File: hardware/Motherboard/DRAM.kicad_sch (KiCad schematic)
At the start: 42 parts, among them U11 74LS245, U12 74LS541, U13 74LS541, U14 74LS541, U15 74LS393, U16 MK4164N, U17 MK4164N, U18 MK4164N, U19 MK4164N, U20 MK4164N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

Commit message: Footprints.
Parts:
- C17, C18, C19, C20, C21, C22, C23, C24, C25, C26, C27, C28, C29, C30, C31, C36, C72: footprint (none) -> Capacitor_THT:C_Disc_D9.0mm_W2.5mm_P5.00mm
- C3, C4: footprint (none) -> Capacitor_THT:C_Disc_D3.0mm_W1.6mm_P2.50mm
- R22, R48: footprint (none) -> Resistor_THT:R_Axial_DIN0309_L9.0mm_D3.2mm_P12.70mm_Horizontal
- U11, U12, U13, U14: footprint (none) -> Package_DIP:DIP-20_W7.62mm_Socket
- U15, U24, U25, U26, U28, U29, U7, U71, U8: footprint (none) -> Package_DIP:DIP-14_W7.62mm_Socket
- U16, U17, U18, U19, U20, U21, U22, U23: footprint Package_DIP:DIP-16_W7.62mm -> Package_DIP:DIP-16_W7.62mm_Socket
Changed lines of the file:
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@@
 			)
 		)
-		(property "Footprint" ""
+		(property "Footprint" "Package_DIP:DIP-14_W7.62mm_Socket"
 			(at 241.3 172.72 0)
 			(effects
@@
 			)
 		)
-		(property "Footprint" "Package_DIP:DIP-16_W7.62mm"
+		(property "Footprint" "Package_DIP:DIP-16_W7.62mm_Socket"
 			(at 363.22 123.698 0)
 			(effects
@@
 			)
 		)
-		(property "Footprint" ""
+		(property "Footprint" "Capacitor_THT:C_Disc_D9.0mm_W2.5mm_P5.00mm"
 			(at 398.4752 49.53 0)
 			(effects
@@
 			)
 		)
-		(property "Footprint" "Package_DIP:DIP-16_W7.62mm"
+		(property "Footprint" "Package_DIP:DIP-16_W7.62mm_Socket"
 			(at 363.22 71.628 0)
 			(effects
@@
 			)
 		)
-		(property "Footprint" "Package_DIP:DIP-16_W7.62mm"
+		(property "Footprint" "Package_DIP:DIP-16_W7.62mm_Socket"
 			(at 294.64 71.628 0)
 			(effects
@@
 			)
 		)
-		(property "Footprint" ""
+		(property "Footprint" "Resistor_THT:R_Axial_DIN0309_L9.0mm_D3.2mm_P12.70mm_Horizontal"
 			(at 90.932 184.15 90)
 			(effects
@@
 			)
 		)
-		(property "Footprint" "Package_DIP:DIP-16_W7.62mm"
+		(property "Footprint" "Package_DIP:DIP-16_W7.62mm_Socket"
 			(at 363.22 175.768 0)
 			(effects
@@
 			)
 		)
-		(property "Footprint" ""
+		(property "Footprint" "Resistor_THT:R_Axial_DIN0309_L9.0mm_D3.2mm_P12.70mm_Horizontal"
 			(at 90.932 224.79 90)
 			(effects
@@
 			)
 		)
-		(property "Footprint" ""
+		(property "Footprint" "Package_DIP:DIP-14_W7.62mm_Socket"
 			(at 266.7 229.87 0)
 			(effects
@@
 			)
 		)
-		(property "Footprint" ""
+		(property "Footprint" "Capacitor_THT:C_Disc_D9.0mm_W2.5mm_P5.00mm"
 			(at 93.6752 102.87 0)
 			(effects
@@
 			)
 		)
-		(property "Footprint" ""
+		(property "Footprint" "Package_DIP:DIP-14_W7.62mm_Socket"
 			(at 266.7 245.11 0)
 			(effects
@@
 			)
 		)
-		(property "Footprint" ""
+		(property "Footprint" "Capacitor_THT:C_Disc_D9.0mm_W2.5mm_P5.00mm"
 			(at 74.6252 102.87 0)
 			(effects
@@
 			)
 		)
-		(property "Footprint" ""
+		(property "Footprint" "Capacitor_THT:C_Disc_D9.0mm_W2.5mm_P5.00mm"
 			(at 176.2252 132.08 0)
 			(effects
@@
 			)
 		)
-		(property "Footprint" ""
+		(property "Footprint" "Package_DIP:DIP-14_W7.62mm_Socket"
 			(at 27.94 158.75 0)
 			(effects
@@
 			)
 		)
-		(property "Footprint" ""
+		(property "Footprint" "Package_DIP:DIP-14_W7.62mm_Socket"
 			(at 241.3 147.32 0)
 			(effects
@@
 			)
 		)
-		(property "Footprint" ""
+		(property "Footprint" "Package_DIP:DIP-20_W7.62mm_Socket"
 			(at 142.24 102.87 0)
 			(effects
@@
 			)
 		)
-		(property "Footprint" ""
+		(property "Footprint" "Package_DIP:DIP-14_W7.62mm_Socket"
 			(at 30.48 241.3 0)
 			(effects
@@
 			)
 		)
-		(property "Footprint" ""
+		(property "Footprint" "Capacitor_THT:C_Disc_D9.0mm_W2.5mm_P5.00mm"
 			(at 78.4352 250.19 0)
 			(effects
@@
 			)
 		)
-		(property "Footprint" ""
+		(property "Footprint" "Package_DIP:DIP-14_W7.62mm_Socket"
 			(at 49.53 241.3 0)
 			(effects
@@
 			)
 		)
-		(property "Footprint" ""
+		(property "Footprint" "Capacitor_THT:C_Disc_D9.0mm_W2.5mm_P5.00mm"
 			(at 266.3952 104.14 0)
 			(effects
@@
 			)
 		)
-		(property "Footprint" ""
+		(property "Footprint" "Package_DIP:DIP-14_W7.62mm_Socket"
 			(at 45.72 190.5 0)
 			(effects
@@
 			)
 		)
-		(property "Footprint" ""
+		(property "Footprint" "Capacitor_THT:C_Disc_D9.0mm_W2.5mm_P5.00mm"
 			(at 266.3952 205.74 0)
 			(effects
@@
 			)
 		)
-		(property "Footprint" ""
+		(property "Footprint" "Package_DIP:DIP-14_W7.62mm_Socket"
 			(at 222.25 271.78 0)
 			(effects
@@
 			)
 		)
-		(property "Footprint" ""
+		(property "Footprint" "Package_DIP:DIP-14_W7.62mm_Socket"
 			(at 76.2 158.75 0)
 			(effects
@@
 			)
 		)
-		(property "Footprint" "Package_DIP:DIP-16_W7.62mm"
+		(property "Footprint" "Package_DIP:DIP-16_W7.62mm_Socket"
 			(at 294.64 175.768 0)
 			(effects
@@
 			)
 		)
-		(property "Footprint" ""
+		(property "Footprint" "Package_DIP:DIP-14_W7.62mm_Socket"
 			(at 114.3 198.12 0)
 			(effects
@@
 			)
 		)
-		(property "Footprint" ""
+		(property "Footprint" "Capacitor_THT:C_Disc_D9.0mm_W2.5mm_P5.00mm"
 			(at 33.9852 102.87 0)
 			(effects
@@
 			)
 		)
-		(property "Footprint" ""
+		(property "Footprint" "Package_DIP:DIP-14_W7.62mm_Socket"
 			(at 114.3 238.76 0)
 			(effects
@@
 			)
 		)
-		(property "Footprint" ""
+		(property "Footprint" "Package_DIP:DIP-14_W7.62mm_Socket"
 			(at 175.26 227.33 0)
 			(effects
@@
 			)
 		)
-		(property "Footprint" ""
+		(property "Footprint" "Capacitor_THT:C_Disc_D9.0mm_W2.5mm_P5.00mm"
 			(at 398.4752 205.74 0)
 			(effects
@@
 			)
 		)
-		(property "Footprint" ""
+		(property "Footprint" "Package_DIP:DIP-14_W7.62mm_Socket"
 			(at 52.07 158.75 0)
 			(effects
@@
 			)
 		)
-		(property "Footprint" ""
+		(property "Footprint" "Package_DIP:DIP-14_W7.62mm_Socket"
 			(at 199.39 227.33 0)
 			(effects
@@
 			)
 		)
-		(property "Footprint" ""
+		(property "Footprint" "Capacitor_THT:C_Disc_D9.0mm_W2.5mm_P5.00mm"
 			(at 398.4752 153.67 0)
 			(effects
@@
 			)
 		)
-		(property "Footprint" ""
+		(property "Footprint" "Package_DIP:DIP-14_W7.62mm_Socket"
 			(at 219.71 227.33 0)
 			(effects
@@
 			)
 		)
-		(property "Footprint" ""
+		(property "Footprint" "Capacitor_THT:C_Disc_D9.0mm_W2.5mm_P5.00mm"
 			(at 266.3952 151.13 0)
 			(effects
@@
 			)
 		)
-		(property "Footprint" ""
+		(property "Footprint" "Capacitor_THT:C_Disc_D9.0mm_W2.5mm_P5.00mm"
 			(at 60.6552 149.86 0)
 			(effects
@@
 			)
 		)
-		(property "Footprint" ""
+		(property "Footprint" "Package_DIP:DIP-14_W7.62mm_Socket"
 			(at 142.24 209.55 0)
 			(effects
@@
 			)
 		)
-		(property "Footprint" ""
+		(property "Footprint" "Package_DIP:DIP-14_W7.62mm_Socket"
 			(at 26.67 118.11 0)
 			(effects
@@
 			)
 		)
-		(property "Footprint" ""
+		(property "Footprint" "Package_DIP:DIP-14_W7.62mm_Socket"
 			(at 46.99 118.11 0)
 			(effects
@@
 			)
 		)
-		(property "Footprint" ""
+		(property "Footprint" "Package_DIP:DIP-14_W7.62mm_Socket"
 			(at 86.36 118.11 0)
 			(effects
@@
 			)
 		)
-		(property "Footprint" ""
+		(property "Footprint" "Capacitor_THT:C_Disc_D9.0mm_W2.5mm_P5.00mm"
 			(at 36.5252 149.86 0)
 			(effects
@@
 			)
 		)
-		(property "Footprint" ""
+		(property "Footprint" "Capacitor_THT:C_Disc_D3.0mm_W1.6mm_P2.50mm"
 			(at 93.6752 195.58 0)
 			(effects
@@
 			)
 		)
-		(property "Footprint" ""
+		(property "Footprint" "Package_DIP:DIP-14_W7.62mm_Socket"
 			(at 246.38 271.78 0)
 			(effects
@@
 			)
 		)
-		(property "Footprint" ""
+		(property "Footprint" "Capacitor_THT:C_Disc_D9.0mm_W2.5mm_P5.00mm"
 			(at 266.3952 53.34 0)
 			(effects
@@
 			)
 		)
-		(property "Footprint" ""
+		(property "Footprint" "Package_DIP:DIP-20_W7.62mm_Socket"
 			(at 190.5 157.48 0)
 			(effects
@@
 			)
 		)
-		(property "Footprint" ""
+		(property "Footprint" "Capacitor_THT:C_Disc_D3.0mm_W1.6mm_P2.50mm"
 			(at 93.6752 236.22 0)
 			(effects
@@
 			)
 		)
-		(property "Footprint" "Package_DIP:DIP-16_W7.62mm"
+		(property "Footprint" "Package_DIP:DIP-16_W7.62mm_Socket"
 			(at 294.64 123.698 0)
 			(effects
@@
 			)
 		)
-		(property "Footprint" ""
+		(property "Footprint" "Package_DIP:DIP-14_W7.62mm_Socket"
 			(at 66.04 241.3 0)
 			(effects
@@
 			)
 		)
-		(property "Footprint" ""
+		(property "Footprint" "Capacitor_THT:C_Disc_D9.0mm_W2.5mm_P5.00mm"
 			(at 54.3052 102.87 0)
 			(effects
@@
 			)
 		)
-		(property "Footprint" ""
+		(property "Footprint" "Package_DIP:DIP-14_W7.62mm_Socket"
 			(at 161.29 266.7 0)
 			(effects
@@
 			)
 		)
-		(property "Footprint" ""
+		(property "Footprint" "Capacitor_THT:C_Disc_D9.0mm_W2.5mm_P5.00mm"
 			(at 398.4752 101.6 0)
 			(effects
@@
 			)
 		)
-		(property "Footprint" ""
+		(property "Footprint" "Package_DIP:DIP-14_W7.62mm_Socket"
 			(at 64.77 209.55 0)
 			(effects
@@
 			)
 		)
-		(property "Footprint" "Package_DIP:DIP-16_W7.62mm"
+		(property "Footprint" "Package_DIP:DIP-16_W7.62mm_Socket"
 			(at 294.64 227.838 0)
 			(effects
@@
 			)
 		)
-		(property "Footprint" ""
+		(property "Footprint" "Capacitor_THT:C_Disc_D9.0mm_W2.5mm_P5.00mm"
 			(at 127.9652 81.28 0)
 			(effects
@@
 			)
 		)
-		(property "Footprint" ""
+		(property "Footprint" "Package_DIP:DIP-20_W7.62mm_Socket"
 			(at 142.24 46.99 0)
 			(effects
@@
 			)
 		)
-		(property "Footprint" ""
+		(property "Footprint" "Package_DIP:DIP-14_W7.62mm_Socket"
 			(at 67.31 118.11 0)
 			(effects
@@
 			)
 		)
-		(property "Footprint" ""
+		(property "Footprint" "Package_DIP:DIP-14_W7.62mm_Socket"
 			(at 204.47 257.81 0)
 			(effects
@@
 			)
 		)
-		(property "Footprint" ""
+		(property "Footprint" "Package_DIP:DIP-20_W7.62mm_Socket"
 			(at 142.24 157.48 0)
 			(effects
@@
 			)
 		)
-		(property "Footprint" "Package_DIP:DIP-16_W7.62mm"
+		(property "Footprint" "Package_DIP:DIP-16_W7.62mm_Socket"
 			(at 363.22 227.838 0)
 			(effects

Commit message: Fix DRAM address bus connection.
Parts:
- U24: footprint Package_DIP:DIP-14_W7.62mm_Socket -> Package_DIP:DIP-16_W7.62mm_Socket
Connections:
- net RA0: now also U16.5 (A0), U17.5 (A0), U18.5 (A0), U19.5 (A0), U20.5 (A0), U21.5 (A0), U22.5 (A0), U23.5 (A0)
- net RA1: now also U16.7 (A1), U17.7 (A1), U18.7 (A1), U19.7 (A1), U20.7 (A1), U21.7 (A1), U22.7 (A1), U23.7 (A1)
- net RA2: now also U16.6 (A2), U17.6 (A2), U18.6 (A2), U19.6 (A2), U20.6 (A2), U21.6 (A2), U22.6 (A2), U23.6 (A2)
- net RA3: now also U16.12 (A3), U17.12 (A3), U18.12 (A3), U19.12 (A3), U20.12 (A3), U21.12 (A3), U22.12 (A3), U23.12 (A3)
- net RA4: now also U16.11 (A4), U17.11 (A4), U18.11 (A4), U19.11 (A4), U20.11 (A4), U21.11 (A4), U22.11 (A4), U23.11 (A4)
- net RA5: now also U16.10 (A5), U17.10 (A5), U18.10 (A5), U19.10 (A5), U20.10 (A5), U21.10 (A5), U22.10 (A5), U23.10 (A5)
- net RA6: now also U16.13 (A6), U17.13 (A6), U18.13 (A6), U19.13 (A6), U20.13 (A6), U21.13 (A6), U22.13 (A6), U23.13 (A6)
- net RA7: now also U16.9 (A7), U17.9 (A7), U18.9 (A7), U19.9 (A7), U20.9 (A7), U21.9 (A7), U22.9 (A7), U23.9 (A7)

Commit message: Fix DRAM address bits ordering.
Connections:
- net RA0: now also U16.13 (A6), U17.13 (A6), U19.13 (A6), U20.13 (A6), U21.13 (A6), U22.13 (A6), U23.13 (A6); no longer U16.5 (A0), U17.5 (A0), U18.5 (A0), U19.5 (A0), U20.5 (A0), U21.5 (A0), U22.5 (A0), U23.5 (A0)
- net RA1: now also U16.12 (A3), U17.12 (A3), U19.12 (A3), U20.12 (A3), U21.12 (A3), U22.12 (A3), U23.12 (A3); no longer U16.7 (A1), U17.7 (A1), U18.7 (A1), U19.7 (A1), U20.7 (A1), U21.7 (A1), U22.7 (A1), U23.7 (A1)
- net RA2: now also U16.5 (A0), U17.5 (A0), U19.5 (A0), U20.5 (A0), U21.5 (A0), U22.5 (A0), U23.5 (A0); no longer U16.6 (A2), U17.6 (A2), U18.6 (A2), U19.6 (A2), U20.6 (A2), U21.6 (A2), U22.6 (A2), U23.6 (A2)
- net RA3: now also U16.11 (A4), U17.11 (A4), U19.11 (A4), U20.11 (A4), U21.11 (A4), U22.11 (A4), U23.11 (A4); no longer U16.12 (A3), U17.12 (A3), U18.12 (A3), U19.12 (A3), U20.12 (A3), U21.12 (A3), U22.12 (A3), U23.12 (A3)
- net RA4: now also U16.6 (A2), U17.6 (A2), U19.6 (A2), U20.6 (A2), U21.6 (A2), U22.6 (A2), U23.6 (A2); no longer U16.11 (A4), U17.11 (A4), U18.11 (A4), U19.11 (A4), U20.11 (A4), U21.11 (A4), U22.11 (A4), U23.11 (A4)
- net RA5: no longer U18.10 (A5)
- net RA6: now also U16.7 (A1), U17.7 (A1), U19.7 (A1), U20.7 (A1), U21.7 (A1), U22.7 (A1), U23.7 (A1); no longer U16.13 (A6), U17.13 (A6), U18.13 (A6), U19.13 (A6), U20.13 (A6), U21.13 (A6), U22.13 (A6), U23.13 (A6)
- net RA7: no longer U18.9 (A7)

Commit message: missing addresses?
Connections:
- net RA0: now also U18.13 (A6)
- net RA1: now also U18.12 (A3)
- net RA2: now also U18.5 (A0)
- net RA3: now also U18.11 (A4)
- net RA4: now also U18.6 (A2)
- net RA5: now also U18.10 (A5)
- net RA6: now also U18.7 (A1)
- net RA7: now also U18.9 (A7)

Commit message: more fixes !
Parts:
- C28: now not fitted
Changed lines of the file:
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@@
 		(in_bom yes)
 		(on_board yes)
-		(dnp no)
+		(dnp yes)
 		(fields_autoplaced yes)
 		(property "Reference" "C28"

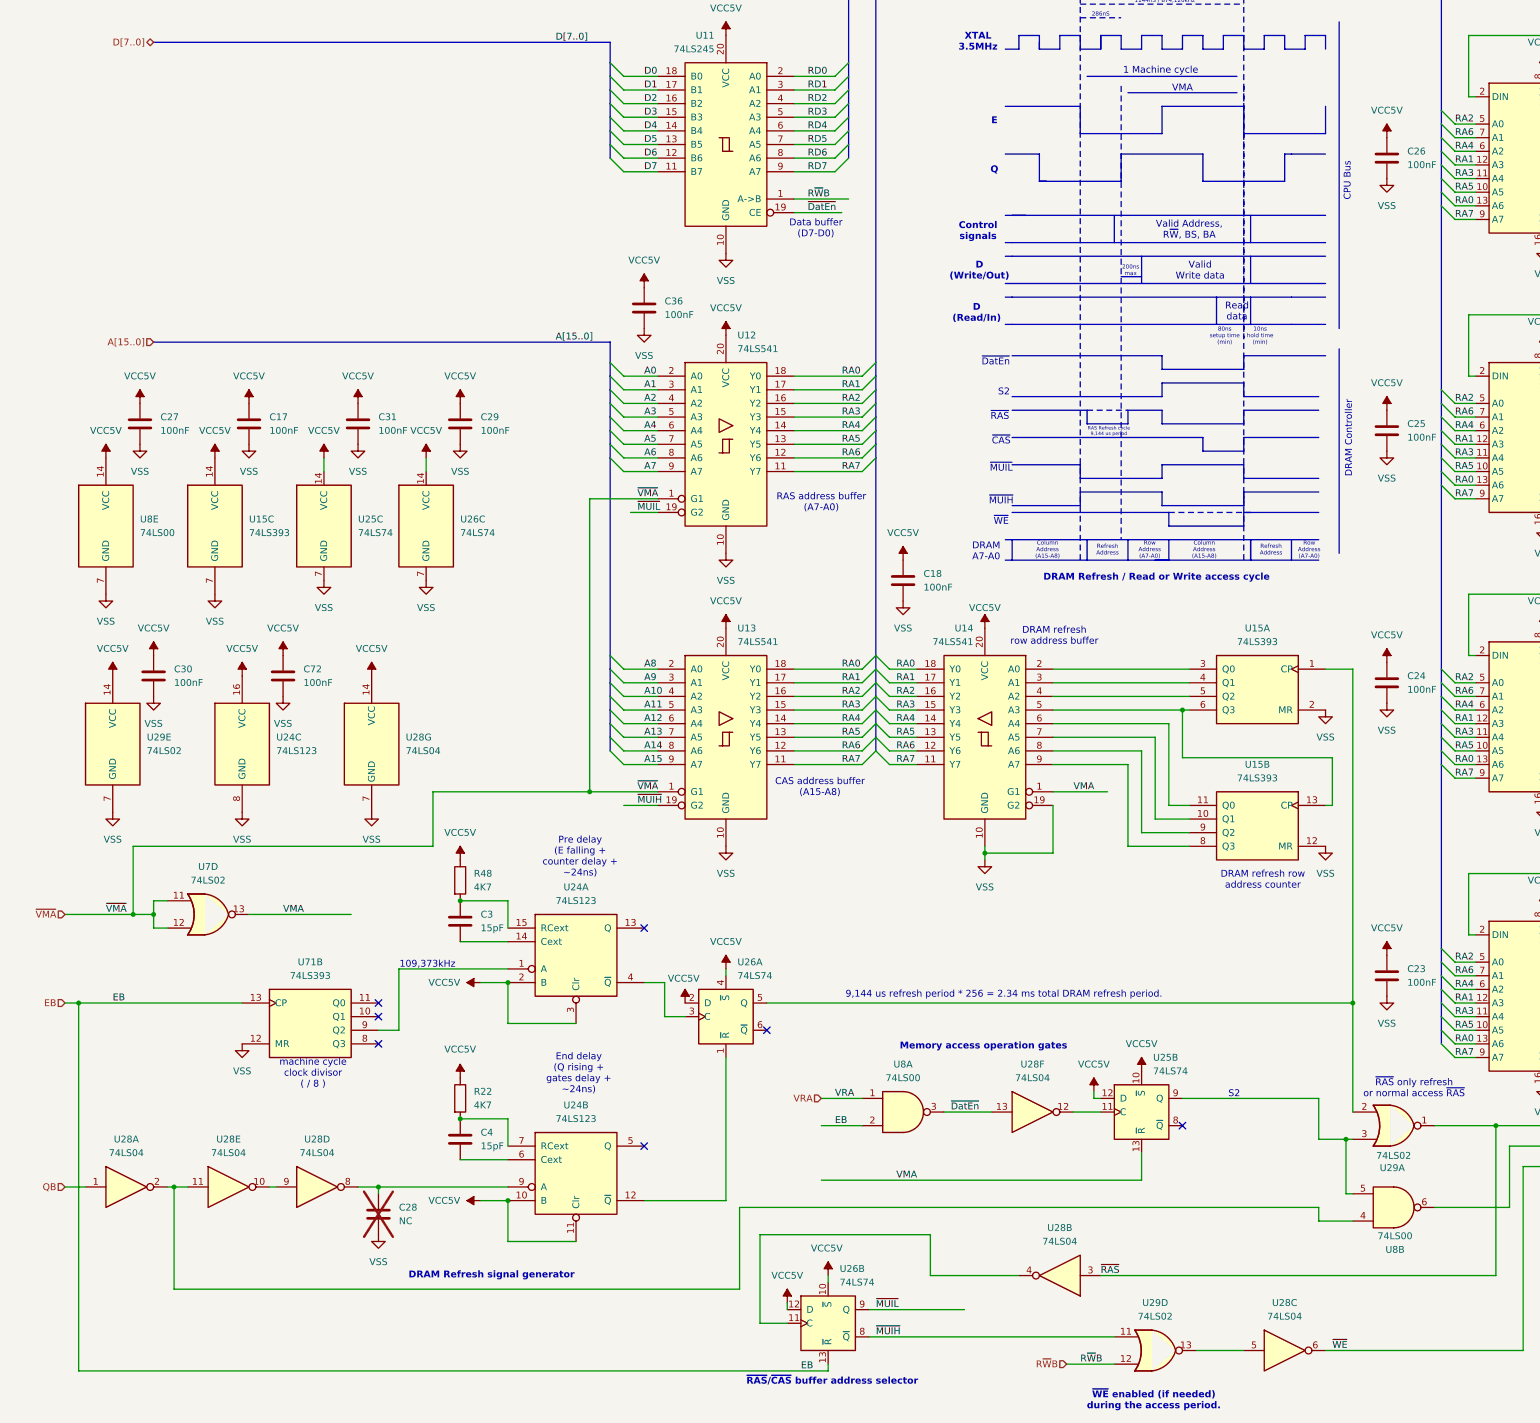
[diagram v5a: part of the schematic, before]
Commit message: add some descriptions / comments.
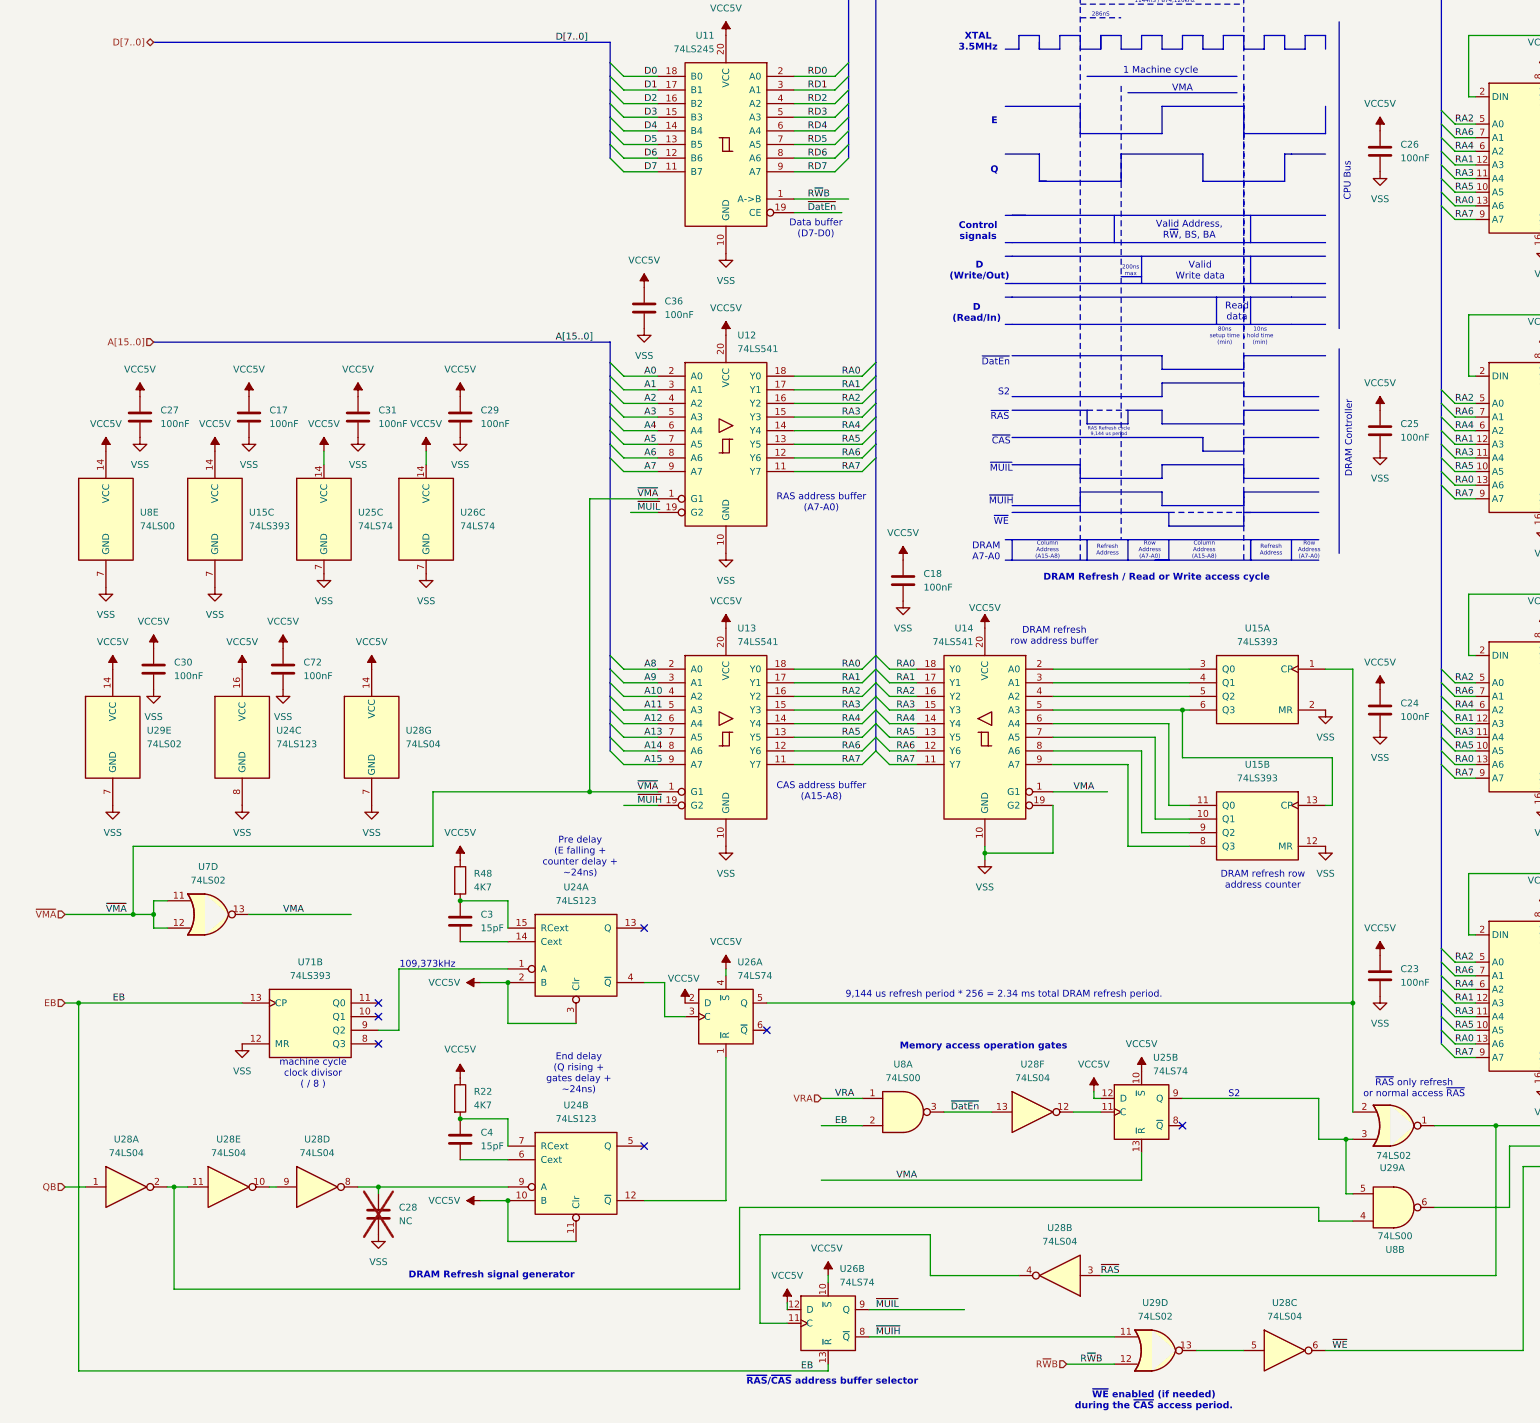
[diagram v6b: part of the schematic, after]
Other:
- note added: "~{RAS}/~{CAS} address buffer selector"
- note added: "~{WE} enabled (if needed) during the ~{CAS} access period."
- note removed: "~{RAS}/~{CAS} buffer address selector"
- note removed: "~{WE} enabled (if needed) during the access period."
- moved on the sheet: C17, C23, C24, C25, C26, C27, C29, C30, C31, C72, U15C, U24C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
